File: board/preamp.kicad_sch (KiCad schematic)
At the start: 10 parts, among them U5 MAX4062

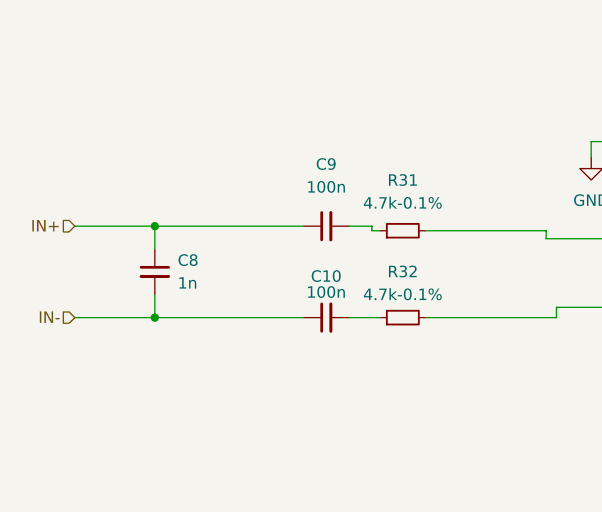
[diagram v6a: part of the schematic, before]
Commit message: reduce balanced out volume, 3.3V supply on SMD for lower emissions
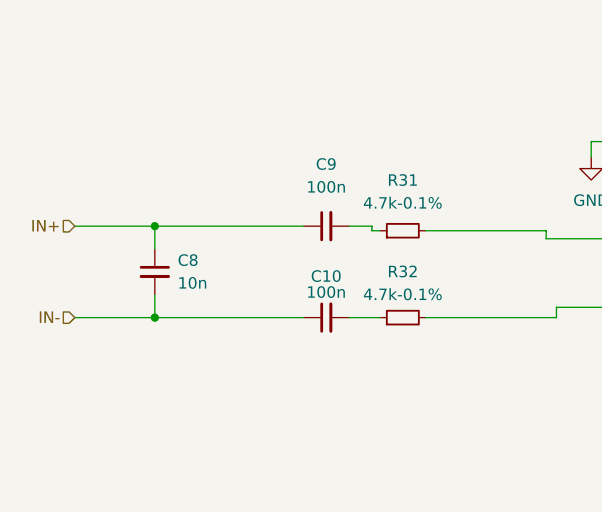
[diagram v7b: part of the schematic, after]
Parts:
- C8: value 1n -> 10n
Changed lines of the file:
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@@
 			)
 		)
-		(property "Value" "1n"
+		(property "Value" "10n"
 			(at 115.57 86.36 0)
 			(effects

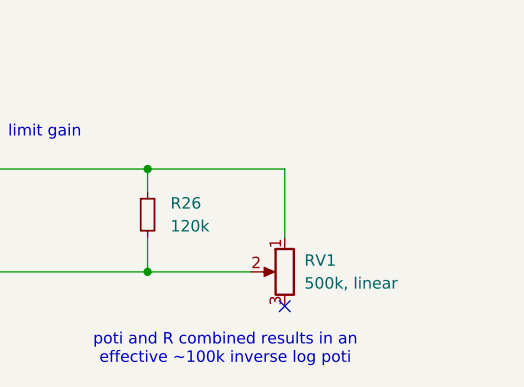
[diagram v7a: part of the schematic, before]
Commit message: rotate potentiometer by 180deg
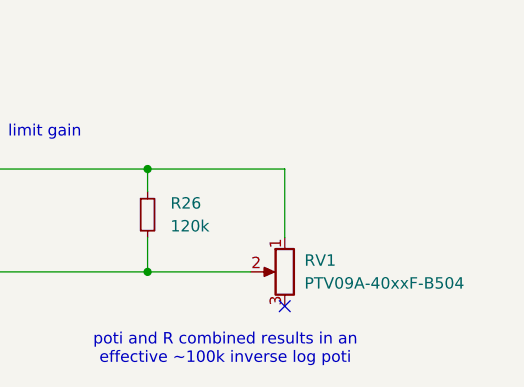
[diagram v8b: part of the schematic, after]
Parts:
- RV1: value 500k, linear -> PTV09A-40xxF-B504
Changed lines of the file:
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@@
 			)
 		)
-		(property "Value" "500k, linear"
+		(property "Value" "PTV09A-40xxF-B504"
 			(at 258.7244 100.33 0)
 			(effects
